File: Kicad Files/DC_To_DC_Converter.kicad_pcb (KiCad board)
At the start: 2 copper layers, 63.5 x 48.3 mm, 12 parts, among them J1 Screw_Terminal_01x02, J2 USB_A, U1 LM2576S-5

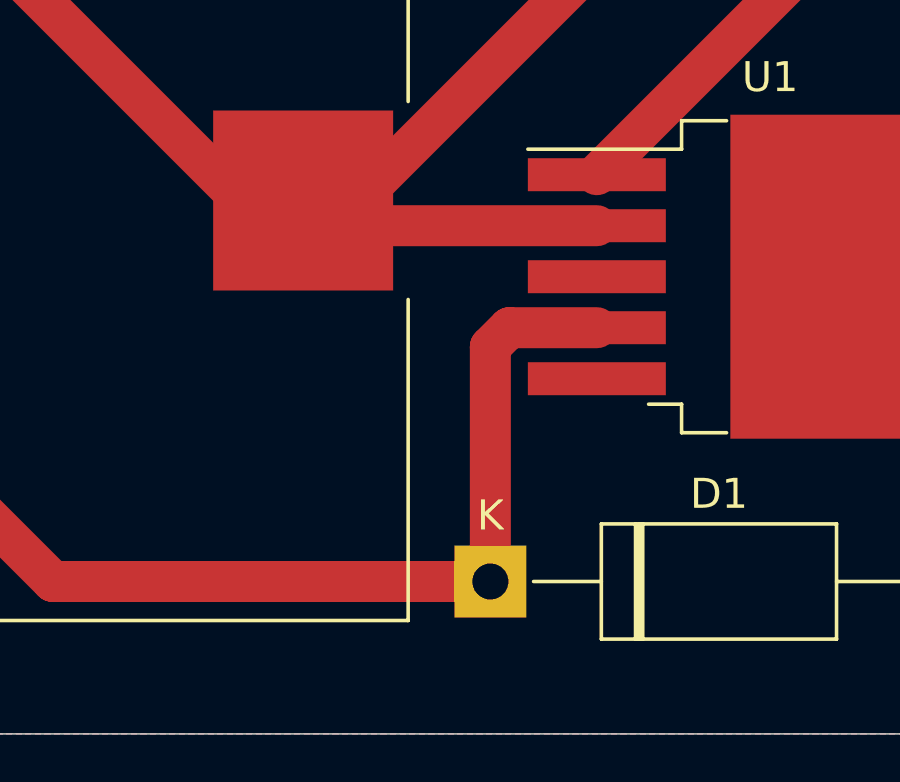
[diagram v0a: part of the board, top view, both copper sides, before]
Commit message: Fixed Problem on the schematic
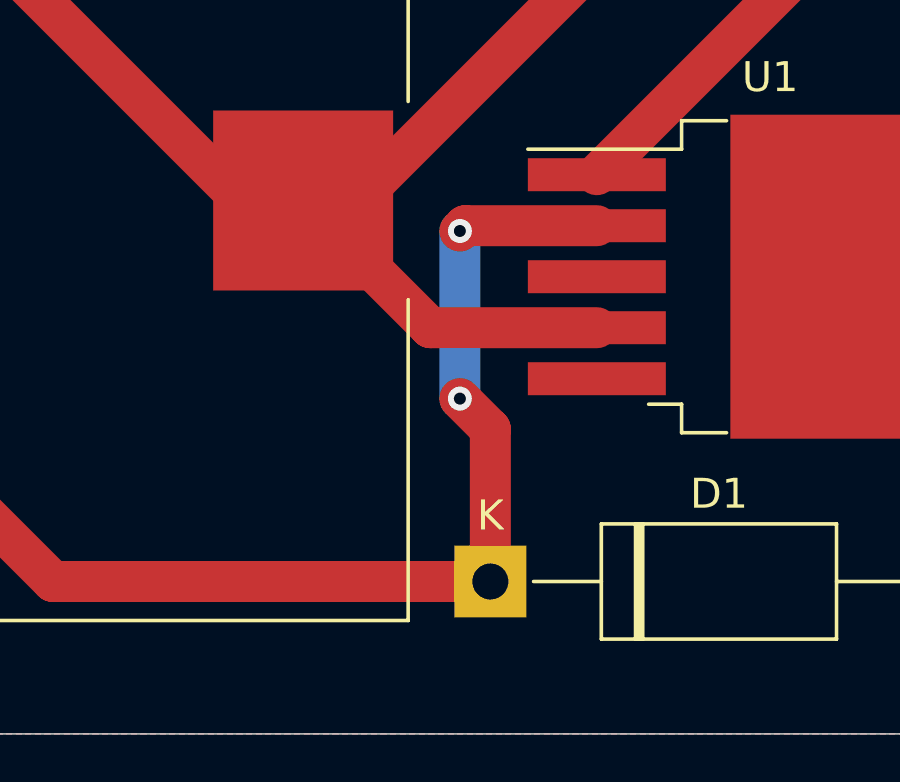
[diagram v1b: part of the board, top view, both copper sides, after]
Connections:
- U1 pad 2: /5V -> Net-(D1-Pad1)
- U1 pad 4: Net-(D1-Pad1) -> /5V
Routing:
- net Net-(D1-Pad1): track 39.9 -> 45.0 mm, vias 0 -> 2
- net /5V: track 76.2 -> 77.6 mm
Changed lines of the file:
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@@
       (net 1 "Net-(C1-Pad1)") (pinfunction "VIN") (pintype "power_in"))
     (pad "2" smd rect (at -5.775 -1.7) (size 4.6 1.1) (layers "F.Cu" "F.Paste" "F.Mask")
-      (net 3 "/5V") (pinfunction "OUT") (pintype "output"))
+      (net 4 "Net-(D1-Pad1)") (pinfunction "OUT") (pintype "output"))
     (pad "3" smd rect (at -5.775 0) (size 4.6 1.1) (layers "F.Cu" "F.Paste" "F.Mask")
       (net 2 "GND") (pinfunction "GND") (pintype "power_in"))
@@
       (net 2 "GND") (pinfunction "GND") (pintype "power_in"))
     (pad "4" smd rect (at -5.775 1.7) (size 4.6 1.1) (layers "F.Cu" "F.Paste" "F.Mask")
-      (net 4 "Net-(D1-Pad1)") (pinfunction "FB") (pintype "input"))
+      (net 3 "/5V") (pinfunction "FB") (pintype "input"))
     (pad "5" smd rect (at -5.775 3.4) (size 4.6 1.1) (layers "F.Cu" "F.Paste" "F.Mask")
       (net 2 "GND") (pinfunction "~{ON}/OFF") (pintype "input"))
@@
   (segment (start 142.875 55.88) (end 155.9 42.855) (width 1.36703) (layer "F.Cu") (net 3))
   (segment (start 130.048 31.496) (end 136.0405 31.496) (width 0.25) (layer "F.Cu") (net 3))
-  (segment (start 141.92 56.72) (end 150.87 56.72) (width 1.36703) (layer "F.Cu") (net 3))
+  (segment (start 145.32 60.12) (end 150.87 60.12) (width 1.36703) (layer "F.Cu") (net 3))
   (segment (start 127 34.544) (end 130.048 31.496) (width 0.25) (layer "F.Cu") (net 3))
   (segment (start 141.08 55.88) (end 142.875 55.88) (width 1.36703) (layer "F.Cu") (net 3))
   (segment (start 127 43.84) (end 127 35.56) (width 1.36703) (layer "F.Cu") (net 3))
-  (segment (start 141.08 55.88) (end 141.92 56.72) (width 1.36703) (layer "F.Cu") (net 3))
+  (segment (start 141.08 55.88) (end 145.32 60.12) (width 1.36703) (layer "F.Cu") (net 3))
   (segment (start 155.9 42.855) (end 155.9 40.92) (width 1.36703) (layer "F.Cu") (net 3))
   (segment (start 136.144 31.5995) (end 141.224 31.5995) (width 0.25) (layer "F.Cu") (net 3))
   (segment (start 139.04 55.88) (end 127 43.84) (width 1.36703) (layer "F.Cu") (net 3))
+  (segment (start 147.32 63.5) (end 146.304 62.484) (width 1.36703) (layer "F.Cu") (net 4))
   (segment (start 147.32 68.58) (end 132.74 68.58) (width 1.36703) (layer "F.Cu") (net 4))
-  (segment (start 147.32 68.58) (end 147.32 60.753948) (width 1.36703) (layer "F.Cu") (net 4))
+  (segment (start 146.48 56.72) (end 150.87 56.72) (width 1.36703) (layer "F.Cu") (net 4))
   (segment (start 132.74 68.58) (end 123.08 58.92) (width 1.36703) (layer "F.Cu") (net 4))
-  (segment (start 147.953948 60.12) (end 150.87 60.12) (width 1.36703) (layer "F.Cu") (net 4))
-  (segment (start 147.32 60.753948) (end 147.953948 60.12) (width 1.36703) (layer "F.Cu") (net 4))
+  (segment (start 146.304 56.896) (end 146.48 56.72) (width 1.36703) (layer "F.Cu") (net 4))
+  (segment (start 147.32 68.58) (end 147.32 63.5) (width 1.36703) (layer "F.Cu") (net 4))
+  (via (at 146.304 56.896) (size 0.8) (drill 0.4) (layers "F.Cu" "B.Cu") (net 4))
+  (via (at 146.304 62.484) (size 0.8) (drill 0.4) (layers "F.Cu" "B.Cu") (net 4))
+  (segment (start 146.304 62.484) (end 146.304 56.896) (width 1.36703) (layer "B.Cu") (net 4))
   (segment (start 175.26 40.64) (end 170.18 35.56) (width 1.36703) (layer "F.Cu") (net 5))
   (segment (start 175.26 66.04) (end 175.26 40.64) (width 1.36703) (layer "F.Cu") (net 5))
